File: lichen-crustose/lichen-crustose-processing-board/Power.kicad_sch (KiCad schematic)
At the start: 10 parts, among them U1 LM4040-2.5

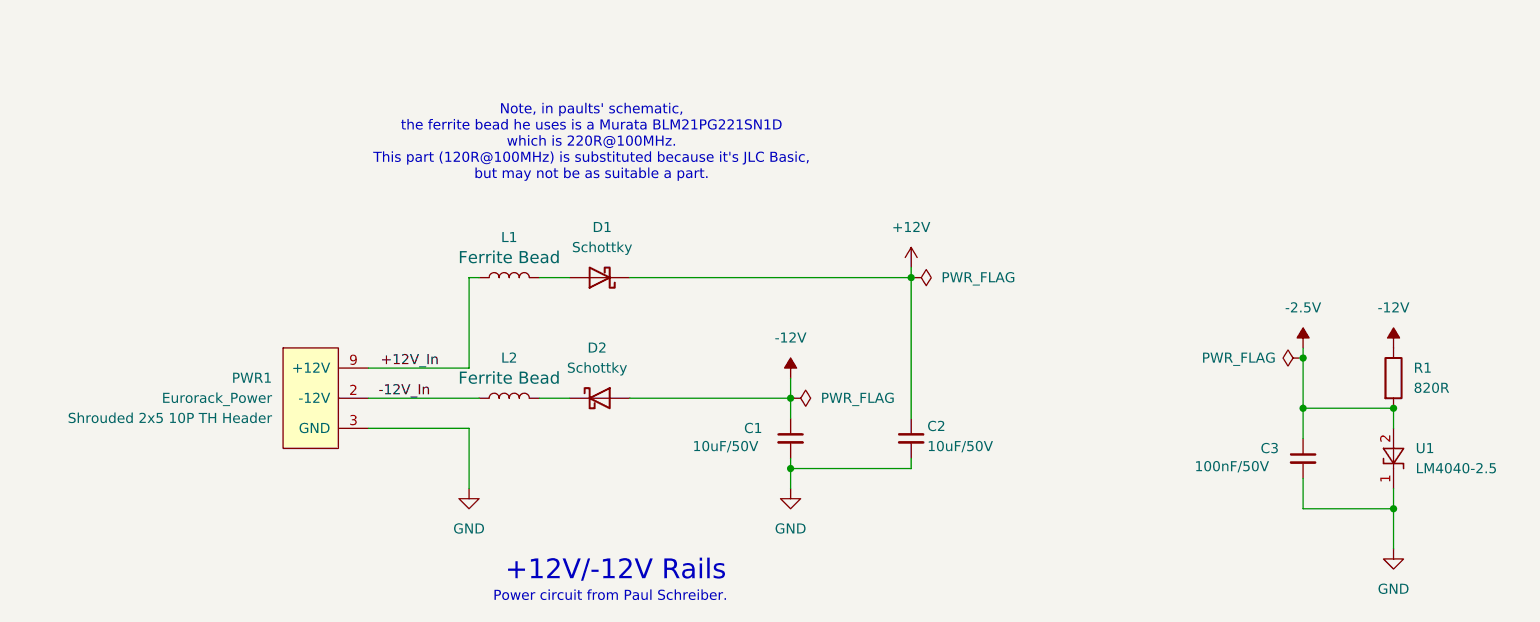
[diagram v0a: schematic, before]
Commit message: feat: Updates Crustose, Cladonia and YouMe Transformer. Adds Stereo Latencies.
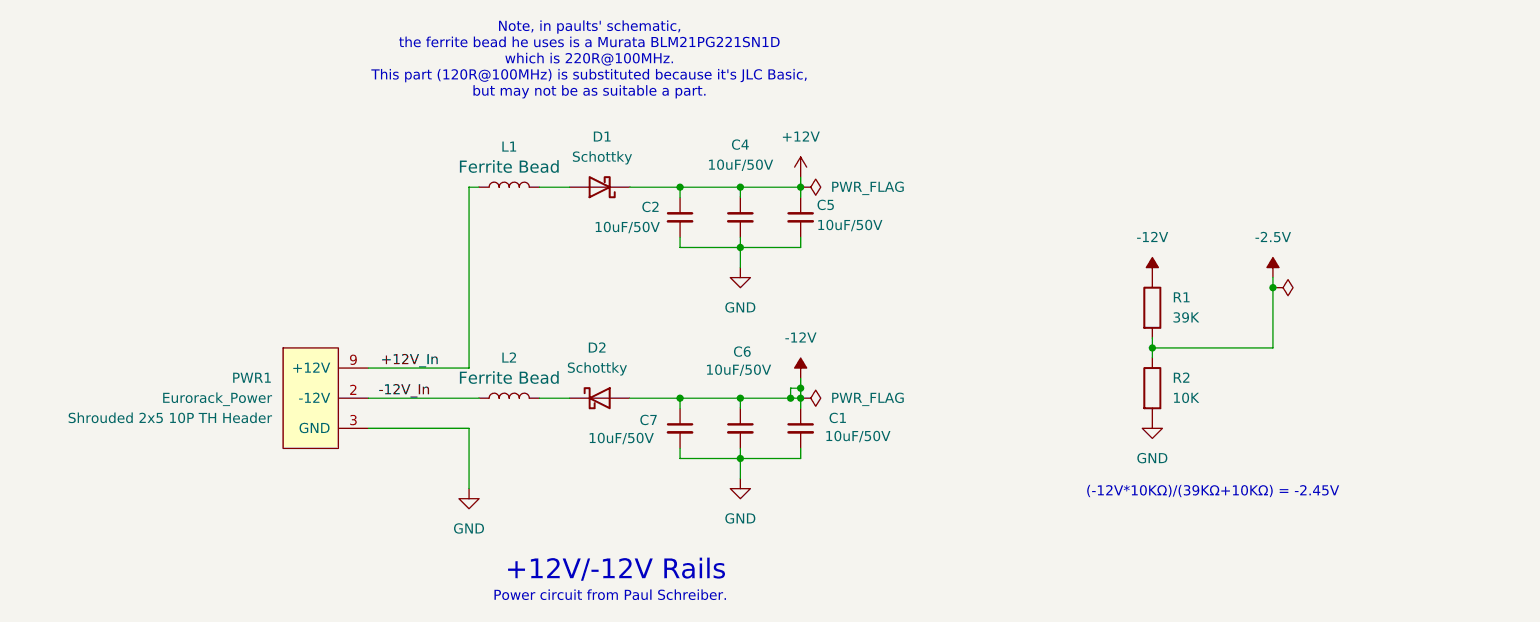
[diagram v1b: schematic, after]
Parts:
- removed C3: 100nF_0603_50V, Lichen:C_0603, symbol Lichen:100nF_0603_50V
- removed R1: 470R_0603, Lichen:R_0603, symbol Lichen:820R_0603
- removed U1: LM4040-2.5, PCM_4ms_Package_SOT:SOT23-3_PO132, symbol PCM_4ms_Reference:LM4040-2.5V
- added C4, C5, C6, C7: 10uF, Lichen:C_0805, symbol Lichen:10uF_0805_50V
- added R1: 39K, Lichen:R_0603, symbol Lichen:39K_0603
- added R2: 10K, Lichen:R_0603, symbol Lichen:10k_0603
- C1, C2: value 10uF_0805_25V -> 10uF; Specifications 50V 10uF X5R ±10% 0805 MLCC SMD -> (none)
- D1: footprint Diode_SMD:D_SMB_Handsoldering -> Diode_SMD:D_SMA_Handsoldering; symbol Lichen:Schottky_Diode -> Lichen:Schottky_Diode_JLC_Basic; JLCPCB ID C222239 -> (none); LCSC (none) -> C8678; Manufacturer STMicroelectronics -> MDD(Microdiode Semiconductor); Part Number STPS1L30U -> SS34
- D2: footprint Diode_SMD:D_SMB_Handsoldering -> Diode_SMD:D_SMA_Handsoldering; symbol Lichen:Schottky_Diode -> Lichen:Schottky_Diode_JLC_Basic; JLCPCB ID C222239 -> (none); LCSC C222239 -> C8678; Manufacturer STMicroelectronics -> MDD(Microdiode Semiconductor); Part Number STPS1L30U -> SS34
- L1, L2: Specifications 120Ω@100MHz 2A 50mΩ ±25% 0603 Ferrite Beads -> (none)
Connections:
- net +12V: now also C4.1, C5.1
- net -12V: now also C6.1, C7.1, R1.1
- net -2.5V: now also R1.2, R2.1
- net GND: now also C4.2, C5.2, C6.2, C7.2, R2.2
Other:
- note added: "(-12V*10KΩ)/(39KΩ+10KΩ) = -2.45V"
- moved on the sheet: C1, C2, D1, L1
